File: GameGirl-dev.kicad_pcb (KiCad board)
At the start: 4 copper layers, 95 x 95 mm, 62 parts, among them J1 USB_C_Receptacle_USB2.0, J2 2.54-connector, J3 FH28-40S-0.5SH(07), SW1 TS-1187, SW10 SKRRAAE, SW2 TS-1187, SW3 TS-1187, SW4 TS-1187, SW5 SKRRAAE, SW6 SKRRAAE, SW7 SKRRAAE, SW8 SKRRAAE, SW9 SKRRAAE, U1 SRV05, U2 STM32F411CEUx, U3 AMS1117-3.3, Y1 Crystal_GND24_Small

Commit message: last modifs before fabrication
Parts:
- D1, D2: footprint LED_SMD:LED_0805_2012Metric -> LED_SMD:LED_0603_1608Metric
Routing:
- net GND: track 67.9 -> 68.9 mm, vias 260 -> 270
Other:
- board text added: "3V3"
- board text added: "A"
- board text added: "B"
- board text added: "BOOT0"
- board text added: "GND"
- board text added: "Power"
- board text added: "SELECT"
- board text added: "START"
- board text added: "SWCLK"
- board text added: "SWIO"
- board text added: "https://github.com/FTOD/GameGirl-DEV-HD"
- board text added: "~NRST"

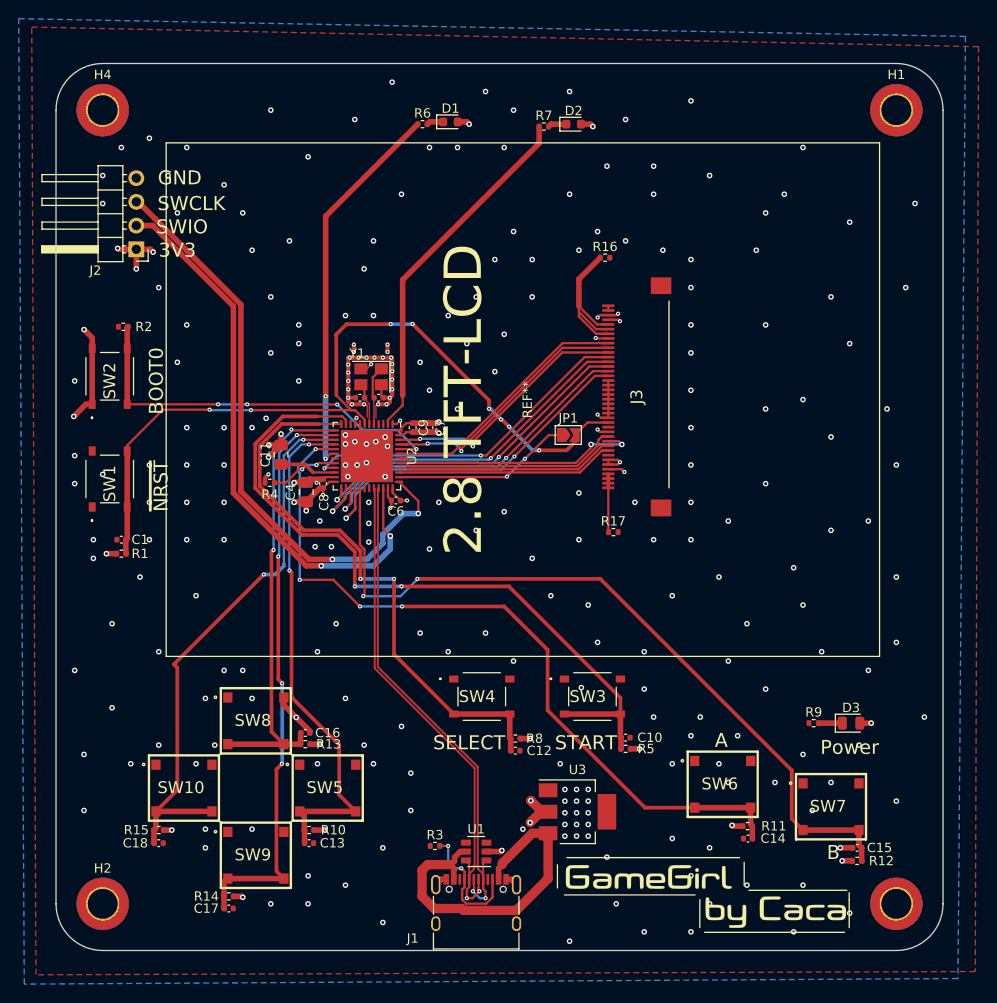
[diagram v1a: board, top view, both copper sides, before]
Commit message: add schematic pdf, some changes to pcb
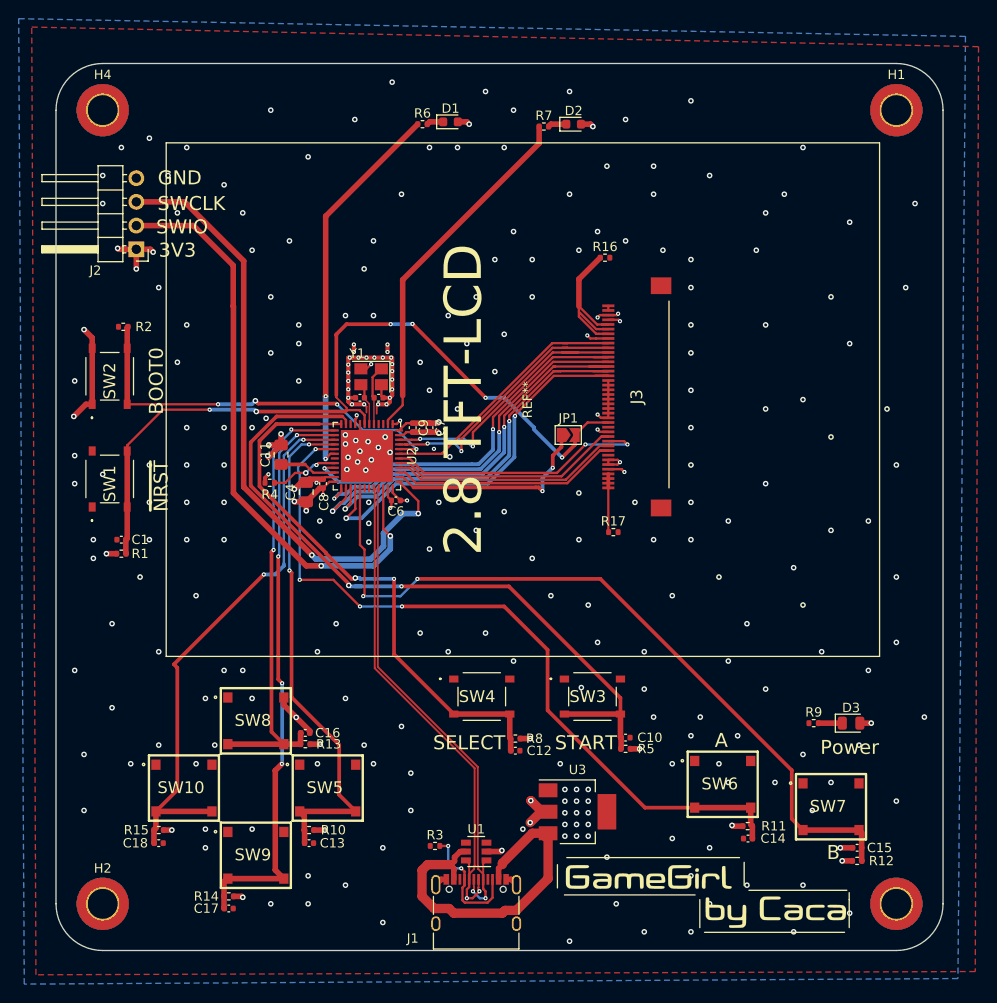
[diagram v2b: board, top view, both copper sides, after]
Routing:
- net /DB4: track 36.5 -> 41.3 mm
- net /DB1: track 37.3 -> 41.7 mm
- net /DB2: track 39.5 -> 43.5 mm
- net /~SCR_NRST: track 19.3 -> 22.9 mm
- net /DB0: track 39.1 -> 42.1 mm
- net /SWCLK: track 64.6 -> 67.5 mm
- net /SWDIO: track 61.6 -> 64.1 mm
- net /DB3: track 36.6 -> 39.0 mm
- net /DB5: track 27.2 -> 29.5 mm
- net /LCD_Connector/~WRX: track 26.7 -> 28.6 mm
- net /LCD_Connector/~CSX: track 23.4 -> 25.2 mm
- net /DB6: track 27.6 -> 29.0 mm
- net /SELECT: track 61.4 -> 60.1 mm
- net /LCD_Connector/~RDX: track 24.2 -> 25.5 mm
- net +3V3: track 57.5 -> 58.8 mm
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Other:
- net class Default: clearance 0.09 -> 0.12
- net class USB_DATA: clearance 0.09 -> 0.12
- rule trace_clearance: 0.09 -> 0.12
- rule trace_min: 0.09 -> 0.12
